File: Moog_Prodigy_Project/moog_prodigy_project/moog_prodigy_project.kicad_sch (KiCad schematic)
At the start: 0 parts

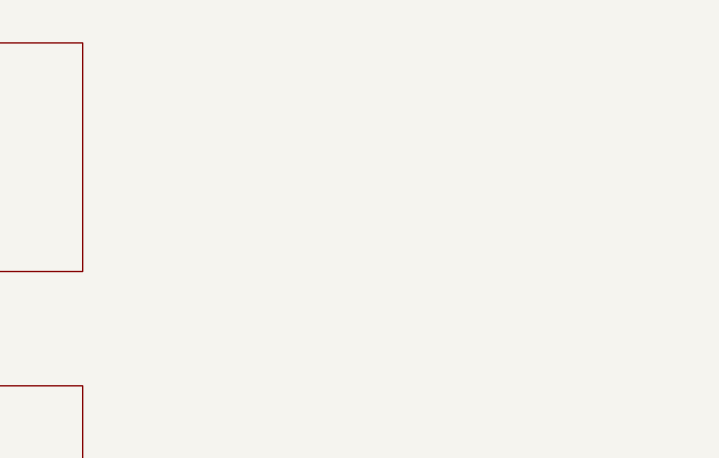
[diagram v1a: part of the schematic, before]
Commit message: Middle part of left side update 20.03.2026
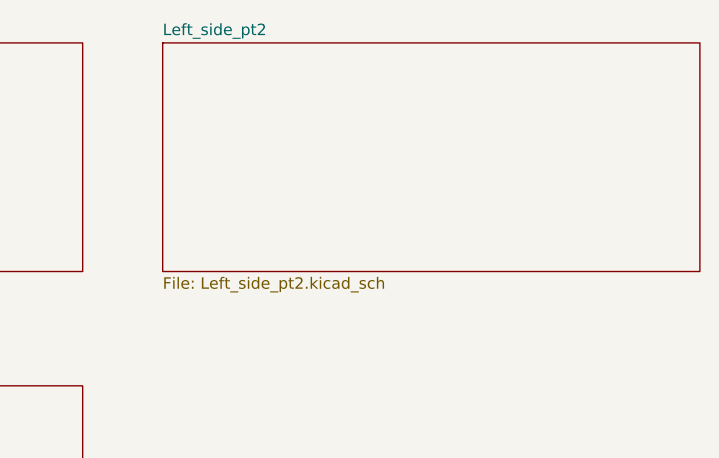
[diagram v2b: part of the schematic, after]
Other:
- added sheet Left_side_pt2 (Left_side_pt2.kicad_sch)
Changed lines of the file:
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@@
+	)
+	(sheet
+		(at 102.87 27.94)
+		(size 59.69 25.4)
+		(exclude_from_sim no)
+		(in_bom yes)
+		(on_board yes)
+		(dnp no)
+		(fields_autoplaced yes)
+		(stroke
+			(width 0.1524)
+			(type solid)
+		)
+		(fill
+			(color 0 0 0 0.0000)
+		)
+		(property "Sheetname" "Left_side_pt2"
+			(at 102.87 27.2284 0)
+			(effects
+				(font
+					(size 1.27 1.27)
+				)
+				(justify left bottom)
+			)
+		)
+		(property "Sheetfile" "Left_side_pt2.kicad_sch"
+			(at 102.87 53.9246 0)
+			(effects
+				(font
+					(size 1.27 1.27)
+				)
+				(justify left top)
+			)
+		)
+		(instances
+			(project "moog_prodigy_project"
+				(path "/db469bdb-b6c3-4a16-9199-d4e6b8d556e8"
+					(page "4")
+				)
+			)
+		)
 	)
 	(sheet

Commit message: Final part of left side 26.03.2026
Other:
- added sheet Left_side_pt3 (Left_side_pt3.kicad_sch)
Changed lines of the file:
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@@
+		)
+	)
+	(sheet
+		(at 171.45 27.94)
+		(size 57.15 25.4)
+		(exclude_from_sim no)
+		(in_bom yes)
+		(on_board yes)
+		(dnp no)
+		(fields_autoplaced yes)
+		(stroke
+			(width 0.1524)
+			(type solid)
+		)
+		(fill
+			(color 0 0 0 0.0000)
+		)
+		(property "Sheetname" "Left_side_pt3"
+			(at 171.45 27.2284 0)
+			(effects
+				(font
+					(size 1.27 1.27)
+				)
+				(justify left bottom)
+			)
+		)
+		(property "Sheetfile" "Left_side_pt3.kicad_sch"
+			(at 171.45 53.9246 0)
+			(effects
+				(font
+					(size 1.27 1.27)
+				)
+				(justify left top)
+			)
+		)
+		(instances
+			(project "moog_prodigy_project"
+				(path "/db469bdb-b6c3-4a16-9199-d4e6b8d556e8"
+					(page "5")
+				)
+			)
 		)
 	)
